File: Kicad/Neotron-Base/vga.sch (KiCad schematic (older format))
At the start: 16 parts, among them J201 DE15HD SVGA Socket, U201 THS7316

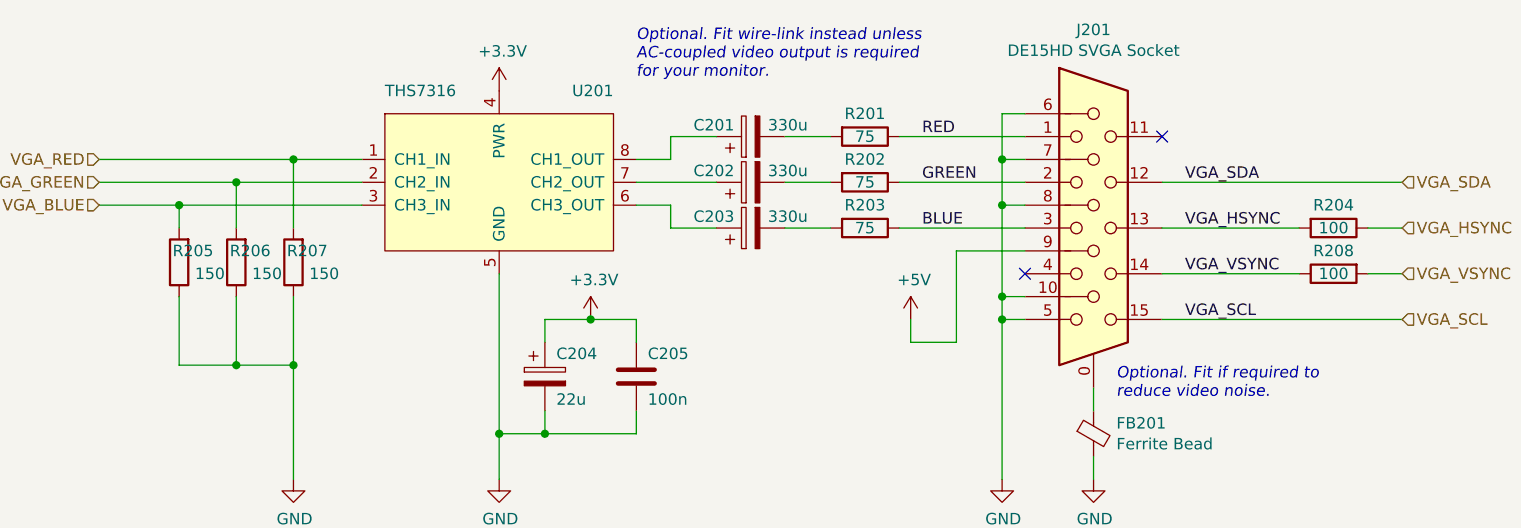
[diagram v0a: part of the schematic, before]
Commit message: Re-work CPU interface to include RMII.
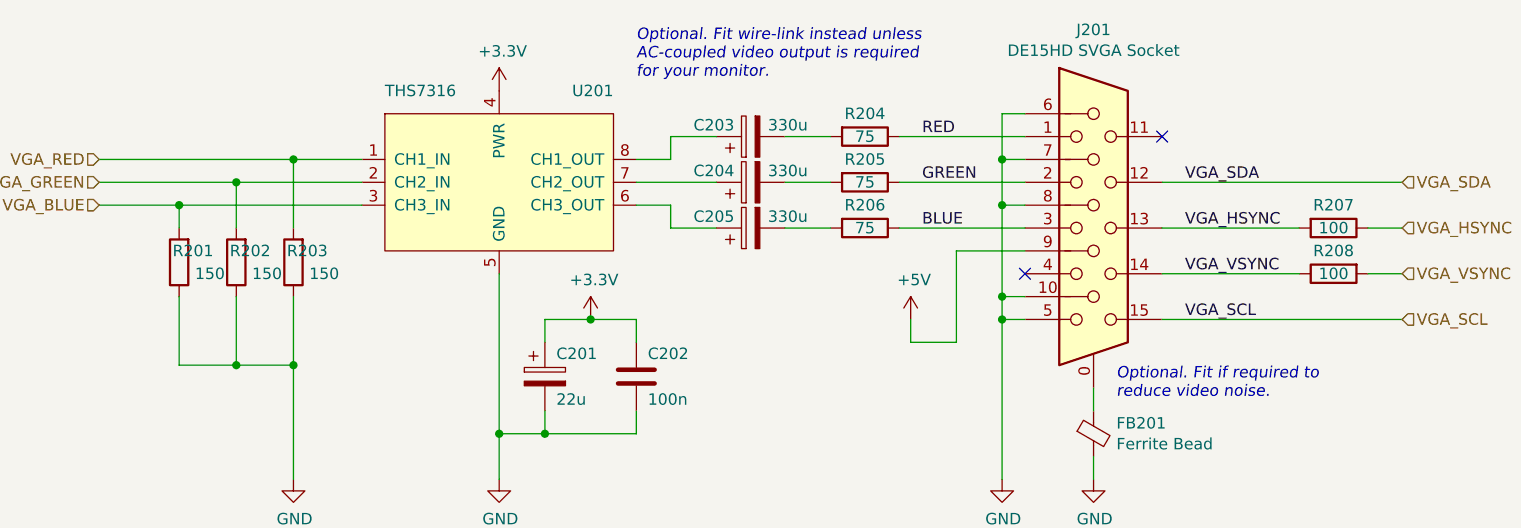
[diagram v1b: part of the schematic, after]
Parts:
- renumbered C204 to C201, C205 to C202, C201 to C203, C202 to C204, C203 to C205, R205 to R201, R206 to R202, R207 to R203, R201 to R204, R202 to R205, R203 to R206, R204 to R207
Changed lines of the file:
@@
 $Descr A4 11693 8268
 encoding utf-8
-Sheet 2 7
+Sheet 2 10
 Title "Neotron Base - VGA Output"
-Date "2020-08-07"
+Date "2020-08-15"
 Rev "[Uncontrolled]"
 Comp "github.com/neotron-compute"
@@
 P 7950 3300
 AR Path="/5F378457" Ref="R?"  Part="1"
-AR Path="/5F373616/5F378457" Ref="R204"  Part="1"
-F 0 "R204" V 7850 3300 50  0000 C CNN
+AR Path="/5F373616/5F378457" Ref="R207"  Part="1"
+F 0 "R207" V 7850 3300 50  0000 C CNN
 F 1 "100" V 7950 3300 50  0000 C CNN
 F 2 "Resistor_THT:R_Axial_DIN0207_L6.3mm_D2.5mm_P10.16mm_Horizontal" V 7880 3300 50  0001 C CNN
@@
 P 5900 2900
 AR Path="/5F37846D" Ref="R?"  Part="1"
-AR Path="/5F373616/5F37846D" Ref="R201"  Part="1"
-F 0 "R201" V 5800 2900 50  0000 C CNN
+AR Path="/5F373616/5F37846D" Ref="R204"  Part="1"
+F 0 "R204" V 5800 2900 50  0000 C CNN
 F 1 "75" V 5900 2900 50  0000 C CNN
 F 2 "Resistor_THT:R_Axial_DIN0207_L6.3mm_D2.5mm_P10.16mm_Horizontal" V 5830 2900 50  0001 C CNN
@@
 P 5900 3100
 AR Path="/5F378473" Ref="R?"  Part="1"
-AR Path="/5F373616/5F378473" Ref="R202"  Part="1"
-F 0 "R202" V 5800 3100 50  0000 C CNN
+AR Path="/5F373616/5F378473" Ref="R205"  Part="1"
+F 0 "R205" V 5800 3100 50  0000 C CNN
 F 1 "75" V 5900 3100 50  0000 C CNN
 F 2 "Resistor_THT:R_Axial_DIN0207_L6.3mm_D2.5mm_P10.16mm_Horizontal" V 5830 3100 50  0001 C CNN
@@
 P 5900 3300
 AR Path="/5F378479" Ref="R?"  Part="1"
-AR Path="/5F373616/5F378479" Ref="R203"  Part="1"
-F 0 "R203" V 5800 3300 50  0000 C CNN
+AR Path="/5F373616/5F378479" Ref="R206"  Part="1"
+F 0 "R206" V 5800 3300 50  0000 C CNN
 F 1 "75" V 5900 3300 50  0000 C CNN
 F 2 "Resistor_THT:R_Axial_DIN0207_L6.3mm_D2.5mm_P10.16mm_Horizontal" V 5830 3300 50  0001 C CNN
@@
 P 5400 2900
 AR Path="/5F3784B5" Ref="C?"  Part="1"
-AR Path="/5F373616/5F3784B5" Ref="C201"  Part="1"
-F 0 "C201" V 5450 3150 50  0000 R CNN
+AR Path="/5F373616/5F3784B5" Ref="C203"  Part="1"
+F 0 "C203" V 5450 3150 50  0000 R CNN
 F 1 "330u" V 5450 2650 50  0000 L CNN
 F 2 "" H 5438 2750 50  0001 C CNN
@@
 P 5400 3300
 AR Path="/5F3784C8" Ref="C?"  Part="1"
-AR Path="/5F373616/5F3784C8" Ref="C203"  Part="1"
-F 0 "C203" V 5450 3550 50  0000 R CNN
+AR Path="/5F373616/5F3784C8" Ref="C205"  Part="1"
+F 0 "C205" V 5450 3550 50  0000 R CNN
 F 1 "330u" V 5450 3050 50  0000 L CNN
 F 2 "" H 5438 3150 50  0001 C CNN
@@
 P 4900 3950
 AR Path="/5F3784CE" Ref="C?"  Part="1"
-AR Path="/5F373616/5F3784CE" Ref="C205"  Part="1"
-F 0 "C205" H 4950 4050 50  0000 L CNN
+AR Path="/5F373616/5F3784CE" Ref="C202"  Part="1"
+F 0 "C202" H 4950 4050 50  0000 L CNN
 F 1 "100n" H 4950 3850 50  0000 L CNN
 F 2 "" H 4938 3800 50  0001 C CNN
@@
 P 4500 3950
 AR Path="/5F3784D4" Ref="C?"  Part="1"
-AR Path="/5F373616/5F3784D4" Ref="C204"  Part="1"
-F 0 "C204" H 4550 4050 50  0000 L CNN
+AR Path="/5F373616/5F3784D4" Ref="C201"  Part="1"
+F 0 "C201" H 4550 4050 50  0000 L CNN
 F 1 "22u" H 4550 3850 50  0000 L CNN
 F 2 "" H 4538 3800 50  0001 C CNN
@@
 P 5400 3100
 AR Path="/5F3784C2" Ref="C?"  Part="1"
-AR Path="/5F373616/5F3784C2" Ref="C202"  Part="1"
-F 0 "C202" V 5450 3350 50  0000 R CNN
+AR Path="/5F373616/5F3784C2" Ref="C204"  Part="1"
+F 0 "C204" V 5450 3350 50  0000 R CNN
 F 1 "330u" V 5450 2850 50  0000 L CNN
 F 2 "" H 5438 2950 50  0001 C CNN
@@
 P 2900 3450
 AR Path="/5F3A45F1" Ref="R?"  Part="1"
-AR Path="/5F373616/5F3A45F1" Ref="R205"  Part="1"
-F 0 "R205" H 2750 3400 50  0000 L CNN
+AR Path="/5F373616/5F3A45F1" Ref="R201"  Part="1"
+F 0 "R201" H 2750 3400 50  0000 L CNN
 F 1 "150" H 2700 3500 50  0000 L CNN
 F 2 "Resistor_THT:R_Axial_DIN0207_L6.3mm_D2.5mm_P10.16mm_Horizontal" V 2830 3450 50  0001 C CNN
@@
 P 3150 3450
 AR Path="/5F3A4DF1" Ref="R?"  Part="1"
-AR Path="/5F373616/5F3A4DF1" Ref="R206"  Part="1"
-F 0 "R206" H 3000 3400 50  0000 L CNN
+AR Path="/5F373616/5F3A4DF1" Ref="R202"  Part="1"
+F 0 "R202" H 3000 3400 50  0000 L CNN
 F 1 "150" H 2950 3500 50  0000 L CNN
 F 2 "Resistor_THT:R_Axial_DIN0207_L6.3mm_D2.5mm_P10.16mm_Horizontal" V 3080 3450 50  0001 C CNN
@@
 P 3400 3450
 AR Path="/5F3A4FA0" Ref="R?"  Part="1"
-AR Path="/5F373616/5F3A4FA0" Ref="R207"  Part="1"
-F 0 "R207" H 3250 3400 50  0000 L CNN
+AR Path="/5F373616/5F3A4FA0" Ref="R203"  Part="1"
+F 0 "R203" H 3250 3400 50  0000 L CNN
 F 1 "150" H 3200 3500 50  0000 L CNN
 F 2 "Resistor_THT:R_Axial_DIN0207_L6.3mm_D2.5mm_P10.16mm_Horizontal" V 3330 3450 50  0001 C CNN
